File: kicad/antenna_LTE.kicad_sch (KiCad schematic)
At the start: 1 part, among them J9 SMA_CONNECTOR

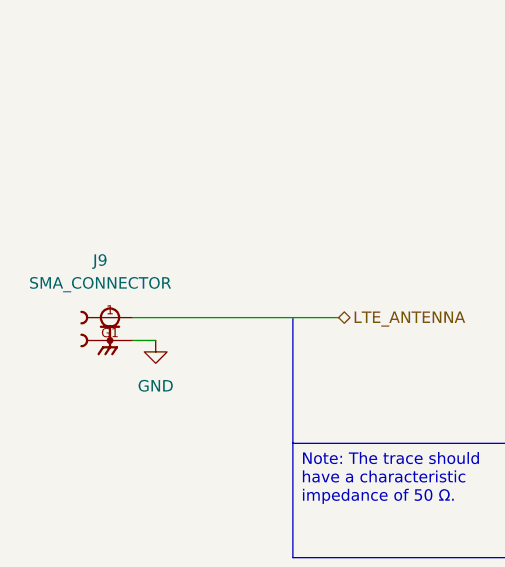
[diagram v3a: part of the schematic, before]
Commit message: feat(PCB): set component-placement example on PCB
This pr will fail due to DRC, skip this and lets have a conversation
about the placement only

Signed-off-by: Bobo Bäck Engström <bobo@id8-engineering.io>
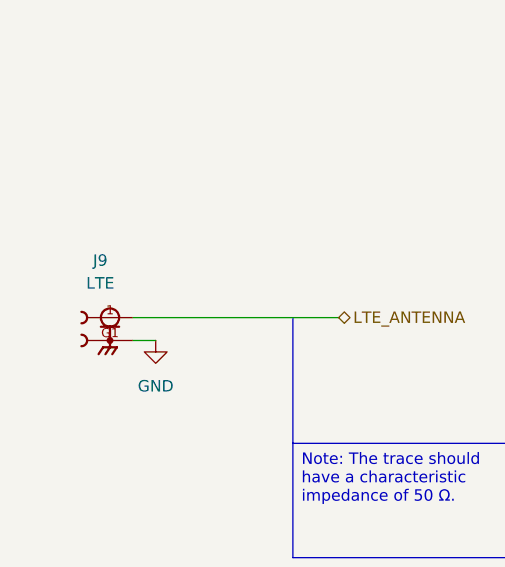
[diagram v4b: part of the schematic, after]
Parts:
- J9: value SMA_CONNECTOR -> LTE; Availability In Stock -> (none); Check_prices https://www.snapeda.com/parts/SMA%20CONNECTOR/LPRS/view-par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 -> (none); Description_1 RF Coaxial Straight SMA Connector -> (none); MANUFACTURER LPRS -> (none); MAXIMUM_PACKAGE_HEIGHT 8.3 mm -> (none); MF LPRS -> (none); MP SMA CONNECTOR -> (none); MPN (none) -> 2081679-1; PARTREV 1.3 -> (none); Package None -> (none); Price None -> (none); Purchase-URL https://www.snapeda.com/api/url_track_click_mouser/?unipart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 -> (none); STANDARD Manufacturer Recommendations -> (none); SnapEDA_Link https://www.snapeda.com/parts/SMA%20CONNECTOR/LPRS/view-par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 -> (none)
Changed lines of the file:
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@@
 (kicad_sch
-	(version 20250114)
+	(version 20260306)
 	(generator "eeschema")
-	(generator_version "9.0")
+	(generator_version "10.0")
 	(paper "A4")
 	(text "\n\n"
@@
 		(at 74.93 90.17 0)
 		(unit 1)
+		(body_style 1)
 		(exclude_from_sim no)
 		(in_bom yes)
 		(on_board yes)
+		(in_pos_files yes)
 		(dnp no)
 		(fields_autoplaced yes)
 		(property "Reference" "J9"
 			(at 73.8505 83.82 0)
-			(effects
-				(font
-					(size 1.27 1.27)
-				)
-			)
-		)
-		(property "Value" "SMA_CONNECTOR"
+			(show_name no)
+			(do_not_autoplace no)
+			(effects
+				(font
+					(size 1.27 1.27)
+				)
+			)
+		)
+		(property "Value" "LTE"
 			(at 73.8505 86.36 0)
+			(show_name no)
+			(do_not_autoplace no)
 			(effects
 				(font
@@
 		(property "Footprint" "seven-lib:LPRS_SMA_CONNECTOR"
 			(at 74.93 90.17 0)
+			(hide yes)
+			(show_name no)
+			(do_not_autoplace no)
 			(effects
 				(font
@@
 				)
 				(justify bottom)
-				(hide yes)
 			)
 		)
 		(property "Datasheet" ""
 			(at 74.93 90.17 0)
-			(effects
-				(font
-					(size 1.27 1.27)
-				)
-				(hide yes)
+			(hide yes)
+			(show_name no)
+			(do_not_autoplace no)
+			(effects
+				(font
+					(size 1.27 1.27)
+				)
 			)
 		)
 		(property "Description" ""
 			(at 74.93 90.17 0)
-			(effects
-				(font
-					(size 1.27 1.27)
-				)
-				(hide yes)
-			)
-		)
-		(property "MF" "LPRS"
+			(hide yes)
+			(show_name no)
+			(do_not_autoplace no)
+			(effects
+				(font
+					(size 1.27 1.27)
+				)
+			)
+		)
+		(property "MPN" "2081679-1"
 			(at 74.93 90.17 0)
-			(effects
-				(font
-					(size 1.27 1.27)
-				)
-				(justify bottom)
-				(hide yes)
-			)
-		)
-		(property "MAXIMUM_PACKAGE_HEIGHT" "8.3 mm"
-			(at 74.93 90.17 0)
-			(effects
-				(font
-					(size 1.27 1.27)
-				)
-				(justify bottom)
-				(hide yes)
-			)
-		)
-		(property "Package" "None"
-			(at 74.93 90.17 0)
-			(effects
-				(font
-					(size 1.27 1.27)
-				)
-				(justify bottom)
-				(hide yes)
-			)
-		)
-		(property "Price" "None"
-			(at 74.93 90.17 0)
-			(effects
-				(font
-					(size 1.27 1.27)
-				)
-				(justify bottom)
-				(hide yes)
-			)
-		)
-		(property "Check_prices" "https://www.snapeda.com/parts/SMA%20CONNECTOR/LPRS/view-part/?ref=eda"
-			(at 74.93 90.17 0)
-			(effects
-				(font
-					(size 1.27 1.27)
-				)
-				(justify bottom)
-				(hide yes)
-			)
-		)
-		(property "STANDARD" "Manufacturer Recommendations"
-			(at 74.93 90.17 0)
-			(effects
-				(font
-					(size 1.27 1.27)
-				)
-				(justify bottom)
-				(hide yes)
-			)
-		)
-		(property "PARTREV" "1.3"
-			(at 74.93 90.17 0)
-			(effects
-				(font
-					(size 1.27 1.27)
-				)
-				(justify bottom)
-				(hide yes)
-			)
-		)
-		(property "SnapEDA_Link" "https://www.snapeda.com/parts/SMA%20CONNECTOR/LPRS/view-part/?ref=snap"
-			(at 74.93 90.17 0)
-			(effects
-				(font
-					(size 1.27 1.27)
-				)
-				(justify bottom)
-				(hide yes)
-			)
-		)
-		(property "MP" "SMA CONNECTOR"
-			(at 74.93 90.17 0)
-			(effects
-				(font
-					(size 1.27 1.27)
-				)
-				(justify bottom)
-				(hide yes)
-			)
-		)
-		(property "Purchase-URL" "https://www.snapeda.com/api/url_track_click_mouser/?unipart_id=4703486&manufacturer=LPRS&part_name=SMA CONNECTOR&search_term=None"
-			(at 74.93 90.17 0)
-			(effects
-				(font
-					(size 1.27 1.27)
-				)
-				(justify bottom)
-				(hide yes)
-			)
-		)
-		(property "Description_1" "RF Coaxial Straight SMA Connector"
-			(at 74.93 90.17 0)
-			(effects
-				(font
-					(size 1.27 1.27)
-				)
-				(justify bottom)
-				(hide yes)
-			)
-		)
-		(property "Availability" "In Stock"
-			(at 74.93 90.17 0)
-			(effects
-				(font
-					(size 1.27 1.27)
-				)
-				(justify bottom)
-				(hide yes)
-			)
-		)
-		(property "MANUFACTURER" "LPRS"
-			(at 74.93 90.17 0)
-			(effects
-				(font
-					(size 1.27 1.27)
-				)
-				(justify bottom)
-				(hide yes)
+			(hide yes)
+			(show_name no)
+			(do_not_autoplace no)
+			(effects
+				(font
+					(size 1.27 1.27)
+				)
 			)
 		)
@@
 		)
 		(instances
-			(project ""
+			(project "seven"
 				(path "/8e3cc843-5797-49f3-8b3a-1c11450ccd1e/0b138663-1828-401e-979e-c711580e91a6"
 					(reference "J9")
@@
 		(at 80.01 92.71 0)
 		(unit 1)
+		(body_style 1)
 		(exclude_from_sim no)
 		(in_bom yes)
 		(on_board yes)
+		(in_pos_files yes)
 		(dnp no)
 		(fields_autoplaced yes)
 		(property "Reference" "#PWR018"
 			(at 80.01 99.06 0)
-			(effects
-				(font
-					(size 1.27 1.27)
-				)
-				(hide yes)
+			(hide yes)
+			(show_name no)
+			(do_not_autoplace no)
+			(effects
+				(font
+					(size 1.27 1.27)
+				)
 			)
 		)
 		(property "Value" "GND"
 			(at 80.01 97.79 0)
+			(show_name no)
+			(do_not_autoplace no)
 			(effects
 				(font
@@
 		(property "Footprint" ""
 			(at 80.01 92.71 0)
-			(effects
-				(font
-					(size 1.27 1.27)
-				)
-				(hide yes)
+			(hide yes)
+			(show_name no)
+			(do_not_autoplace no)
+			(effects
+				(font
+					(size 1.27 1.27)
+				)
 			)
 		)
 		(property "Datasheet" ""
 			(at 80.01 92.71 0)
-			(effects
-				(font
-					(size 1.27 1.27)
-				)
-				(hide yes)
+			(hide yes)
+			(show_name no)
+			(do_not_autoplace no)
+			(effects
+				(font
+					(size 1.27 1.27)
+				)
 			)
 		)
 		(property "Description" "Power symbol creates a global label with name \"GND\" , ground"
 			(at 80.01 92.71 0)
-			(effects
-				(font
-					(size 1.27 1.27)
-				)
-				(hide yes)
-			)
-		)
+			(hide yes)
+			(show_name no)
+			(do_not_autoplace no)
+			(effects
+				(font
+					(size 1.27 1.27)
+				)
+			)
+		)
